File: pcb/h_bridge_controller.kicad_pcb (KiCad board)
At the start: 2 copper layers, 118.1 x 55.1 mm, 58 parts, among them P1 PWR_JACK_2.5x5.5, P10 HEADER_02X08_SMD, P11 HEADER_02X08_SMD, P2 HEADER_01X03_SMD_RA, P3 HEADER_01X03_SMD_RA, P4 HEADER_01X03_SMD_RA, P5 HEADER_01X03_SMD_RA, P6 HEADER_01X02_SMD_RA, P7 BNC_DOUBLE_RA, P8 HEADER_02X08_SMD, P9 HEADER_02X08_SMD, SW1 SPST_SLIDE_AS, U1 TLE7230R, U2 TLE7230R, U3 TLE7230R, U4 TLE7230R

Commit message: Progress towards pcb v1.0.
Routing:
- net GND: track 558.3 -> 0.00 mm, vias 1 -> 0
- net VAA: track 217.8 -> 0.00 mm, vias 1 -> 0
- net +5V: track 216.2 -> 0.00 mm, vias 4 -> 0
- net /LED_PWR: track 207.8 -> 0.00 mm, vias 1 -> 0
- net /SCK: track 112.7 -> 0.00 mm, vias 5 -> 0
- net /RESET: track 97.9 -> 0.00 mm, vias 1 -> 0
- net /CS: track 96.8 -> 0.00 mm, vias 2 -> 0
- net /BNC_A: track 91.3 -> 0.00 mm
- net /TX3: track 85.3 -> 0.00 mm
- net /RX0: track 70.0 -> 0.00 mm
- net /RX3: track 65.1 -> 0.00 mm, vias 1 -> 0
- net /MISO: track 62.2 -> 0.00 mm, vias 1 -> 0
- net /SO2: track 61.2 -> 0.00 mm
- net /TX0: track 58.4 -> 0.00 mm
- net /BNC_B: track 56.7 -> 0.00 mm
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- removed copper zone on B.Cu, net GND
- removed copper zone on F.Cu, net VAA
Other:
- board text added: "Janelia Modular Device h_bridge_controller model_number: 1170 03/2016 ver 1.0"
- board text removed: "Janelia Modular Device h_bridge_controller model_number: 1110 03/2016 ver 1.5"

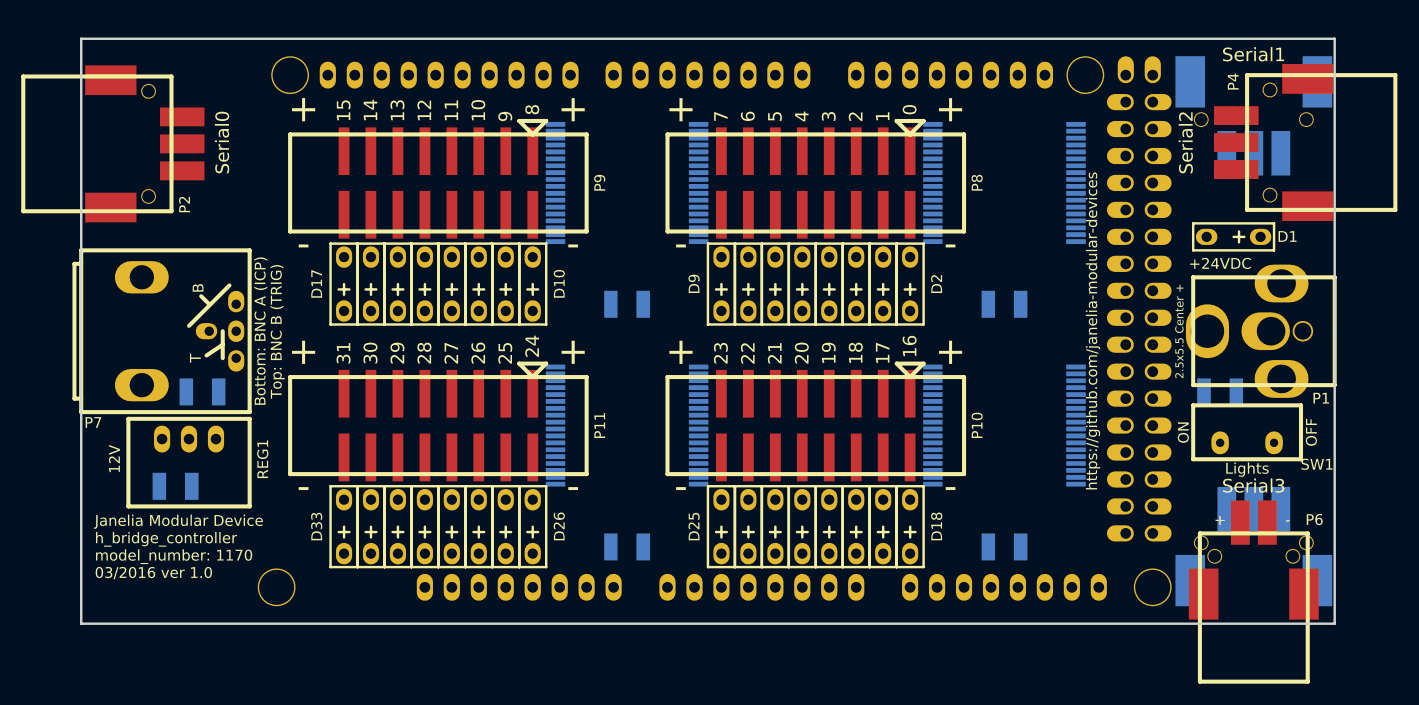
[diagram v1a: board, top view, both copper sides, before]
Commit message: Use relay_controller as pcb base.
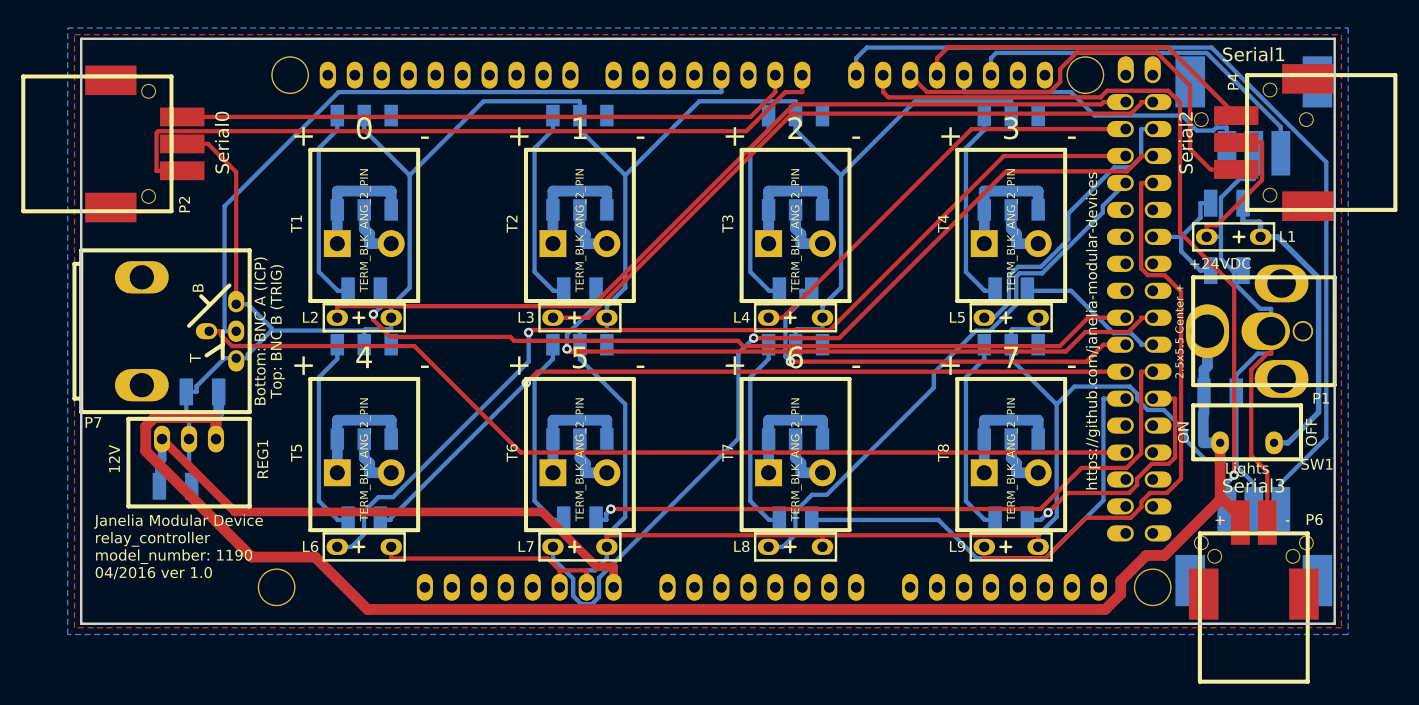
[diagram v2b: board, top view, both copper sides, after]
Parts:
- removed C4, C5, C6, C7: 0.1uF, h_bridge_controller:SM1210
- removed D1, D10, D11, D12, D13, D14, D15, D16, D17, D18, D19, D2, D20, D21, D22, D23, D24, D25, D26, D27, D28, D29, D3, D30, D31, D32, D33, D4, D5, D6, D7, D8, D9: LED_24V, h_bridge_controller:LED_555-3XXX
- removed P10, P11, P8, P9: HEADER_02X08_SMD, h_bridge_controller:HEADER_02x08_SMD
- added L1: LED_24V, relay_controller:LED_555-3XXX, F.Cu at (201.9, 94.0)
- added L2: LED_5V_GRN, relay_controller:LED_555-3XXX, F.Cu at (120.0, 101.6)
- added L3: LED_5V_GRN, relay_controller:LED_555-3XXX, F.Cu at (140.3, 101.6)
- added L4: LED_5V_GRN, relay_controller:LED_555-3XXX, F.Cu at (160.7, 101.6)
- added L5: LED_5V_GRN, relay_controller:LED_555-3XXX, F.Cu at (181.0, 101.6)
- added L6: LED_5V_GRN, relay_controller:LED_555-3XXX, F.Cu at (120.0, 123.2)
- added L7: LED_5V_GRN, relay_controller:LED_555-3XXX, F.Cu at (140.3, 123.2)
- added L8: LED_5V_GRN, relay_controller:LED_555-3XXX, F.Cu at (160.7, 123.2)
- added L9: LED_5V_GRN, relay_controller:LED_555-3XXX, F.Cu at (181.0, 123.2)
- added R1: 5.11k, relay_controller:SM1210, B.Cu at (201.3, 90.8)
- added R10: 150, relay_controller:SM1210, B.Cu at (181.0, 120.7)
- added R2: 1k, relay_controller:SM1210, B.Cu at (201.3, 97.2)
- added R3: 150, relay_controller:SM1210, B.Cu at (120.0, 99.1)
- added R4: 150, relay_controller:SM1210, B.Cu at (140.3, 99.1)
- added R5: 150, relay_controller:SM1210, B.Cu at (160.7, 99.1)
- added R6: 150, relay_controller:SM1210, B.Cu at (181.0, 99.1)
- added R7: 150, relay_controller:SM1210, B.Cu at (120.0, 120.7)
- added R8: 150, relay_controller:SM1210, B.Cu at (140.3, 120.7)
- added R9: 150, relay_controller:SM1210, B.Cu at (160.7, 120.7)
- added T1: TERM_BLK_ANG_2_PIN, relay_controller:TERM_BLK_ANG_2_PIN, F.Cu at (120.0, 94.6)
- added T2: TERM_BLK_ANG_2_PIN, relay_controller:TERM_BLK_ANG_2_PIN, F.Cu at (140.3, 94.6)
- added T3: TERM_BLK_ANG_2_PIN, relay_controller:TERM_BLK_ANG_2_PIN, F.Cu at (160.7, 94.6)
- added T4: TERM_BLK_ANG_2_PIN, relay_controller:TERM_BLK_ANG_2_PIN, F.Cu at (181.0, 94.6)
- added T5: TERM_BLK_ANG_2_PIN, relay_controller:TERM_BLK_ANG_2_PIN, F.Cu at (120.0, 116.2)
- added T6: TERM_BLK_ANG_2_PIN, relay_controller:TERM_BLK_ANG_2_PIN, F.Cu at (140.3, 116.2)
- added T7: TERM_BLK_ANG_2_PIN, relay_controller:TERM_BLK_ANG_2_PIN, F.Cu at (160.7, 116.2)
- added T8: TERM_BLK_ANG_2_PIN, relay_controller:TERM_BLK_ANG_2_PIN, F.Cu at (181.0, 116.2)
- added U5: SSR_DC_6PIN, relay_controller:ASSR-1611, B.Cu at (120.0, 108.6)
- added U6: SSR_DC_6PIN, relay_controller:ASSR-1611, B.Cu at (140.3, 108.6)
- added U7: SSR_DC_6PIN, relay_controller:ASSR-1611, B.Cu at (160.7, 108.6)
- added U8: SSR_DC_6PIN, relay_controller:ASSR-1611, B.Cu at (181.0, 108.6)
- ARDUINO1: footprint h_bridge_controller:ARDUINO_MEGA_SHIELD -> relay_controller:ARDUINO_MEGA_SHIELD
- C1, C2, C3: footprint h_bridge_controller:SM1210 -> relay_controller:SM1210
- P1: footprint h_bridge_controller:DCJACK_2PIN_HIGHCURRENT -> relay_controller:DCJACK_2PIN_HIGHCURRENT
- P2, P3, P4, P5: footprint h_bridge_controller:Header_3_Pin_SMD_RA -> relay_controller:Header_3_Pin_SMD_RA
- P6: footprint h_bridge_controller:Header_2_Pin_SMD_RA -> relay_controller:Header_2_Pin_SMD_RA
- P7: footprint h_bridge_controller:BNC_DOUBLE -> relay_controller:BNC_DOUBLE
- REG1: footprint h_bridge_controller:DC_DC_CONV_R78C -> relay_controller:DC_DC_CONV_R78C
- SW1: footprint h_bridge_controller:SPST_SLIDE_AS -> relay_controller:SPST_SLIDE_AS
- U1, U2, U3, U4: value TLE7230R -> SSR_DC_6PIN; footprint h_bridge_controller:PG-DSO-36 -> relay_controller:ASSR-1611
- moved U1 60.4 mm to (120.0, 87.0)
- moved U4 43.9 mm to (181.0, 87.0)
- moved U3 31.6 mm to (160.7, 87.0)
- moved U2 4.84 mm to (140.3, 87.0)
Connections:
- ARDUINO1 pad 22: (no net) -> /LED_0
- ARDUINO1 pad 23: (no net) -> /LED_1
- ARDUINO1 pad 24: (no net) -> /LED_2
- ARDUINO1 pad 25: (no net) -> /LED_3
- ARDUINO1 pad 26: (no net) -> /LED_4
- ARDUINO1 pad 27: (no net) -> /LED_5
- ARDUINO1 pad 28: (no net) -> /LED_6
- ARDUINO1 pad 29: (no net) -> /LED_7
- ARDUINO1 pad 33: (no net) -> /LED_PWR_IN
- ARDUINO1 pad 38: (no net) -> /RELAY_0
- ARDUINO1 pad 39: (no net) -> /RELAY_1
- ARDUINO1 pad 40: (no net) -> /RELAY_2
- ARDUINO1 pad 41: (no net) -> /RELAY_3
- ARDUINO1 pad 42: (no net) -> /RELAY_4
- ARDUINO1 pad 43: (no net) -> /RELAY_5
- ARDUINO1 pad 44: /RESET -> /RELAY_6
- ARDUINO1 pad 45: (no net) -> /RELAY_7
- ARDUINO1 pad 46: /CS -> (no net)
- ARDUINO1 pad 50: /MISO -> (no net)
- ARDUINO1 pad 51: /MOSI -> (no net)
- ARDUINO1 pad 52: /SCK -> (no net)
- ARDUINO1 pad 5V_1: +5V -> (no net)
- U1 pad 1: GND -> Net-(R3-Pad1)
- U1 pad 2: (no net) -> GND
- U1 pad 4: /OUT0 -> /OUT_0+
- U1 pad 5: /OUT1 -> /OUT_0-
- U1 pad 6: GND -> /OUT_0+
- U2 pad 1: GND -> Net-(R4-Pad1)
- U2 pad 2: (no net) -> GND
- U2 pad 4: /OUT8 -> /OUT_1+
- U2 pad 5: /OUT9 -> /OUT_1-
- U2 pad 6: GND -> /OUT_1+
- U3 pad 1: GND -> Net-(R5-Pad1)
- U3 pad 2: (no net) -> GND
- U3 pad 4: /OUT16 -> /OUT_2+
- U3 pad 5: /OUT17 -> /OUT_2-
- U3 pad 6: GND -> /OUT_2+
- U4 pad 1: GND -> Net-(R6-Pad1)
- U4 pad 2: (no net) -> GND
- U4 pad 4: /OUT24 -> /OUT_3+
- U4 pad 5: /OUT25 -> /OUT_3-
- U4 pad 6: GND -> /OUT_3+
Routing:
- net GND: track 0.00 -> 410.8 mm
- net VAA: track 0.00 -> 149.0 mm
- net /LED_4: track 0.00 -> 92.4 mm, vias 0 -> 1
- net /BNC_A: track 0.00 -> 91.3 mm
- net /TX3: track 0.00 -> 85.2 mm
- net /LED_5: track 0.00 -> 83.6 mm, vias 0 -> 1
- net /LED_0: track 0.00 -> 83.4 mm
- net /RELAY_4: track 0.00 -> 76.1 mm, vias 0 -> 1
- net /RELAY_0: track 0.00 -> 76.1 mm, vias 0 -> 1
- net /RX3: track 0.00 -> 71.2 mm, vias 0 -> 1
- net /RX0: track 0.00 -> 70.0 mm
- net /BNC_B: track 0.00 -> 65.7 mm
- net /LED_1: track 0.00 -> 65.0 mm
- net /RELAY_1: track 0.00 -> 63.4 mm, vias 0 -> 1
- net /RELAY_5: track 0.00 -> 63.1 mm, vias 0 -> 1
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- added copper zone on B.Cu, net GND
- added copper zone on F.Cu, net GND
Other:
- board text added: "Janelia Modular Device relay_controller model_number: 1190 04/2016 ver 1.0"
- board text removed: "10"
- board text removed: "11"
- board text removed: "12"
- board text removed: "13"
- board text removed: "14"
- board text removed: "15"
- board text removed: "16"
- board text removed: "17"
- board text removed: "18"
- board text removed: "19"
- board text removed: "20"
- board text removed: "21"
- board text removed: "22"
- board text removed: "23"
- board text removed: "24"
- board text removed: "25"
- board text removed: "26"
- board text removed: "27"
- board text removed: "28"
- board text removed: "29"
- board text removed: "30"
- board text removed: "31"
- board text removed: "8"
- board text removed: "9"
- board text removed: "Janelia Modular Device h_bridge_controller model_number: 1170 03/2016 ver 1.0"

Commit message: relay_controller -> h_bridge_controller.
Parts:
- ARDUINO1: footprint relay_controller:ARDUINO_MEGA_SHIELD -> h_bridge_controller:ARDUINO_MEGA_SHIELD
- C1, C2, C3, R1, R10, R2, R3, R4, R5, R6, R7, R8, R9: footprint relay_controller:SM1210 -> h_bridge_controller:SM1210
- L1, L2, L3, L4, L5, L6, L7, L8, L9: footprint relay_controller:LED_555-3XXX -> h_bridge_controller:LED_555-3XXX
- P1: footprint relay_controller:DCJACK_2PIN_HIGHCURRENT -> h_bridge_controller:DCJACK_2PIN_HIGHCURRENT
- P2, P3, P4, P5: footprint relay_controller:Header_3_Pin_SMD_RA -> h_bridge_controller:Header_3_Pin_SMD_RA
- P6: footprint relay_controller:Header_2_Pin_SMD_RA -> h_bridge_controller:Header_2_Pin_SMD_RA
- P7: footprint relay_controller:BNC_DOUBLE -> h_bridge_controller:BNC_DOUBLE
- REG1: footprint relay_controller:DC_DC_CONV_R78C -> h_bridge_controller:DC_DC_CONV_R78C
- SW1: footprint relay_controller:SPST_SLIDE_AS -> h_bridge_controller:SPST_SLIDE_AS
- T1, T2, T3, T4, T5, T6, T7, T8: footprint relay_controller:TERM_BLK_ANG_2_PIN -> h_bridge_controller:TERM_BLK_ANG_2_PIN
- U1, U2, U3, U4, U5, U6, U7, U8: footprint relay_controller:ASSR-1611 -> h_bridge_controller:ASSR-1611
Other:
- board text added: "Janelia Modular Device h_bridge_controller model_number: 1190 04/2016 ver 1.0"
- board text removed: "Janelia Modular Device relay_controller model_number: 1190 04/2016 ver 1.0"

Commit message: Progress towards pcb1.0.
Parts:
- removed R10, R5, R6: 150, h_bridge_controller:SM1210
- removed T5, T6, T7, T8: TERM_BLK_ANG_2_PIN, h_bridge_controller:TERM_BLK_ANG_2_PIN
- removed U3, U4, U5, U6, U7, U8: SSR_DC_6PIN, h_bridge_controller:ASSR-1611
- added C4: 0.1uF, h_bridge_controller:SM1210, B.Cu at (121.3, 108.0)
- added C5: 0.1uF, h_bridge_controller:SM1210, B.Cu at (142.9, 108.0)
- added C6: 47uF, h_bridge_controller:SM2917_POL, B.Cu at (114.3, 108.0)
- added C7: 0.1uF, h_bridge_controller:SM1210, B.Cu at (158.8, 108.0)
- added C8: 0.1uF, h_bridge_controller:SM1210, B.Cu at (181.0, 108.0)
- added C9: 47uF, h_bridge_controller:SM2917_POL, B.Cu at (151.8, 108.0)
- added D1: diode_schottky_40V_1A, h_bridge_controller:DO-214AC(SMA), B.Cu at (119.4, 87.6)
- added D10: diode_schottky_40V_1A, h_bridge_controller:DO-214AC(SMA), B.Cu at (157.5, 99.1)
- added D11: diode_schottky_40V_1A, h_bridge_controller:DO-214AC(SMA), B.Cu at (162.6, 87.6)
- added D12: diode_schottky_40V_1A, h_bridge_controller:DO-214AC(SMA), B.Cu at (162.6, 99.1)
- added D13: diode_schottky_40V_1A, h_bridge_controller:DO-214AC(SMA), B.Cu at (176.5, 87.6)
- added D14: diode_schottky_40V_1A, h_bridge_controller:DO-214AC(SMA), B.Cu at (176.5, 99.1)
- added D15: diode_schottky_40V_1A, h_bridge_controller:DO-214AC(SMA), B.Cu at (181.6, 87.6)
- added D16: diode_schottky_40V_1A, h_bridge_controller:DO-214AC(SMA), B.Cu at (181.6, 99.1)
- added D2: diode_schottky_40V_1A, h_bridge_controller:DO-214AC(SMA), B.Cu at (119.4, 99.1)
- added D3: diode_schottky_40V_1A, h_bridge_controller:DO-214AC(SMA), B.Cu at (124.5, 87.6)
- added D4: diode_schottky_40V_1A, h_bridge_controller:DO-214AC(SMA), B.Cu at (124.5, 99.1)
- added D5: diode_schottky_40V_1A, h_bridge_controller:DO-214AC(SMA), B.Cu at (138.4, 87.6)
- added D6: diode_schottky_40V_1A, h_bridge_controller:DO-214AC(SMA), B.Cu at (138.4, 99.1)
- added D7: diode_schottky_40V_1A, h_bridge_controller:DO-214AC(SMA), B.Cu at (143.5, 87.6)
- added D8: diode_schottky_40V_1A, h_bridge_controller:DO-214AC(SMA), B.Cu at (143.5, 99.1)
- added D9: diode_schottky_40V_1A, h_bridge_controller:DO-214AC(SMA), B.Cu at (157.5, 87.6)
- added P10: HEADER_01X05_SMD_SHR, h_bridge_controller:Header_Shrouded_5_Pin_SMD, F.Cu at (175.9, 115.6)
- added P8: HEADER_01X05_SMD_SHR, h_bridge_controller:Header_Shrouded_5_Pin_SMD, F.Cu at (125.1, 115.6)
- added P9: HEADER_01X05_SMD_SHR, h_bridge_controller:Header_Shrouded_5_Pin_SMD, F.Cu at (150.5, 115.6)
- L2, L3, L4, L5, L6, L7, L8, L9: value LED_5V_GRN -> LED_24V
- R1: value 5.11k -> 0.5_2010; footprint h_bridge_controller:SM1210 -> h_bridge_controller:SM2010
- R2: value 1k -> 0.5_2010; footprint h_bridge_controller:SM1210 -> h_bridge_controller:SM2010
- R3, R4: value 150 -> 0.5_2010; footprint h_bridge_controller:SM1210 -> h_bridge_controller:SM2010
- R7, R8, R9: value 150 -> 180
- U1, U2: value SSR_DC_6PIN -> L298; footprint h_bridge_controller:ASSR-1611 -> h_bridge_controller:POWERSO20
- moved R1 84.4 mm to (120.7, 115.6), turned to 270 degrees
- moved R2 61.9 mm to (142.2, 115.6), turned to 270 degrees
- moved L6 46.3 mm to (153.0, 90.8), turned to 0 degrees
- moved R4 43.3 mm to (180.3, 115.6), turned to 270 degrees
- moved R3 42.4 mm to (158.8, 116.2), turned to 270 degrees
- moved L7 42.0 mm to (167.0, 90.8), turned to 0 degrees
- moved U2 37.5 mm to (169.5, 110.5), turned to 90 degrees
- moved L5 34.7 mm to (148.0, 90.8), turned to 0 degrees
- moved L8 34.3 mm to (172.1, 90.8), turned to 0 degrees
- moved L9 32.8 mm to (186.1, 90.8), turned to 0 degrees
- moved L4 28.8 mm to (134.0, 90.8), turned to 0 degrees
- moved U1 26.1 mm to (131.4, 110.5), turned to 90 degrees
- moved R9 17.9 mm to (178.4, 122.6), turned to 180 degrees
- moved L3 15.7 mm to (128.9, 90.8), turned to 0 degrees
- moved R8 12.8 mm to (153.0, 122.6), turned to 180 degrees
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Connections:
- ARDUINO1 pad 10: (no net) -> /PWM_2
- ARDUINO1 pad 11: (no net) -> /PWM_3
- ARDUINO1 pad 2: (no net) -> /SW_2
- ARDUINO1 pad 20: (no net) -> /SW_1
- ARDUINO1 pad 21: (no net) -> /SW_0
- ARDUINO1 pad 22: /LED_0 -> /DIR_0A
- ARDUINO1 pad 23: /LED_1 -> /DIR_0B
- ARDUINO1 pad 24: /LED_2 -> /DIR_1A
- ARDUINO1 pad 25: /LED_3 -> /DIR_1B
- ARDUINO1 pad 26: /LED_4 -> /DIR_2A
- ARDUINO1 pad 27: /LED_5 -> /DIR_2B
- ARDUINO1 pad 28: /LED_6 -> /DIR_3A
- ARDUINO1 pad 29: /LED_7 -> /DIR_3B
- ARDUINO1 pad 33: /LED_PWR_IN -> (no net)
- ARDUINO1 pad 38: /RELAY_0 -> (no net)
- ARDUINO1 pad 39: /RELAY_1 -> (no net)
- ARDUINO1 pad 40: /RELAY_2 -> (no net)
- ARDUINO1 pad 41: /RELAY_3 -> (no net)
- ARDUINO1 pad 42: /RELAY_4 -> (no net)
- ARDUINO1 pad 43: /RELAY_5 -> (no net)
- ARDUINO1 pad 44: /RELAY_6 -> (no net)
- ARDUINO1 pad 45: /RELAY_7 -> (no net)
- ARDUINO1 pad 5V_1: (no net) -> +5V
- ARDUINO1 pad 8: (no net) -> /PWM_0
- ARDUINO1 pad 9: (no net) -> /PWM_1
- ARDUINO1 pad A0: (no net) -> /SENSE_0
- ARDUINO1 pad A1: (no net) -> /SENSE_1
- ARDUINO1 pad A2: (no net) -> /SENSE_2
- ARDUINO1 pad A3: (no net) -> /SENSE_3
- L2 pad 1: /LED_0 -> /LED_PWR
- L2 pad 2: GND -> /OUT_0+
- L3 pad 1: /LED_1 -> /LED_PWR
- L3 pad 2: GND -> /OUT_0-
- L4 pad 1: /LED_2 -> /LED_PWR
- L4 pad 2: GND -> /OUT_1+
- L5 pad 1: /LED_3 -> /LED_PWR
- L5 pad 2: GND -> /OUT_1-
- L6 pad 1: /LED_4 -> /LED_PWR
- L6 pad 2: GND -> /OUT_2+
- L7 pad 1: /LED_5 -> /LED_PWR
- L7 pad 2: GND -> /OUT_2-
- L8 pad 1: /LED_6 -> /LED_PWR
- L8 pad 2: GND -> /OUT_3+
- L9 pad 1: /LED_7 -> /LED_PWR
- L9 pad 2: GND -> /OUT_3-
- R1 pad 1: /LED_PWR -> /SENSE_0
- R1 pad 2: /LED_PWR_IN -> GND
- R2 pad 1: /LED_PWR_IN -> /SENSE_1
- R3 pad 1: Net-(R3-Pad1) -> /SENSE_2
- R3 pad 2: /RELAY_0 -> GND
- R4 pad 1: Net-(R4-Pad1) -> /SENSE_3
- R4 pad 2: /RELAY_1 -> GND
- R7 pad 2: /RELAY_4 -> +5V
- R8 pad 2: /RELAY_5 -> +5V
- R9 pad 2: /RELAY_6 -> +5V
- U1 pad 1: Net-(R3-Pad1) -> GND
- U1 pad 2: GND -> /SENSE_0
- U1 pad 6: /OUT_0+ -> VAA
- U2 pad 1: Net-(R4-Pad1) -> GND
- U2 pad 2: GND -> /SENSE_2
- U2 pad 4: /OUT_1+ -> /OUT_2+
- U2 pad 5: /OUT_1- -> /OUT_2-
- U2 pad 6: /OUT_1+ -> VAA
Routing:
- net GND: track 410.8 -> 0.00 mm
- net VAA: track 149.0 -> 0.00 mm
- net /LED_4: track 92.4 -> 0.00 mm, vias 1 -> 0
- net /BNC_A: track 91.3 -> 0.00 mm
- net /TX3: track 85.2 -> 0.00 mm
- net /LED_5: track 83.6 -> 0.00 mm, vias 1 -> 0
- net /LED_0: track 83.4 -> 0.00 mm
- net /RELAY_4: track 76.1 -> 0.00 mm, vias 1 -> 0
- net /RELAY_0: track 76.1 -> 0.00 mm, vias 1 -> 0
- net /RX3: track 71.2 -> 0.00 mm, vias 1 -> 0
- net /RX0: track 70.0 -> 0.00 mm
- net /BNC_B: track 65.7 -> 0.00 mm
- net /LED_1: track 65.0 -> 0.00 mm
- net /RELAY_1: track 63.4 -> 0.00 mm, vias 1 -> 0
- net /RELAY_5: track 63.1 -> 0.00 mm, vias 1 -> 0
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- removed copper zone on B.Cu, net GND
- removed copper zone on F.Cu, net GND
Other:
- board text added: "Janelia Modular Device h_bridge_controller model_number: 1170 04/2016 ver 1.0"
- board text removed: "2"
- board text removed: "3"
- board text removed: "4"
- board text removed: "5"
- board text removed: "6"
- board text removed: "7"
- board text removed: "Janelia Modular Device h_bridge_controller model_number: 1190 04/2016 ver 1.0"

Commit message: More progress towards pcb1.0.
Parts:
- R1, R2, R3, R4: value 0.5_2010 -> 0.5
- moved L2 5.08 mm to (114.9, 95.9)
- moved L3 5.08 mm to (128.9, 95.9)
- moved L4 5.08 mm to (134.0, 95.9)
- moved L5 5.08 mm to (148.0, 95.9)
- moved L6 5.08 mm to (153.0, 95.9)
- moved L7 5.08 mm to (167.0, 95.9)
- moved L8 5.08 mm to (172.1, 95.9)
- moved L9 5.08 mm to (186.1, 95.9)
- moved C8 2.62 mm to (181.6, 105.4)
- moved C5 2.62 mm to (143.5, 105.4)
- moved C4 2.01 mm to (119.4, 107.3), turned to 90 degrees
- moved C6 2.01 mm to (112.4, 107.3)
- moved R3 1.80 mm to (157.5, 114.9), turned to 180 degrees
- moved R1 1.42 mm to (119.4, 114.9), turned to 180 degrees
- moved R4 1.42 mm to (181.6, 114.9), turned to 0 degrees
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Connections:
- net /PWM_0 renamed /ENABLE_0
- net /PWM_1 renamed /ENABLE_1
- net /PWM_2 renamed /ENABLE_2
- net /PWM_3 renamed /ENABLE_3
- L1 pad 1: /LED_PWR -> VAA
- L1 pad 2: GND -> /LED_GND
- L2 pad 1: /LED_PWR -> /OUT_0+
- L2 pad 2: /OUT_0+ -> /LED_GND
- L3 pad 1: /LED_PWR -> /OUT_0-
- L3 pad 2: /OUT_0- -> /LED_GND
- L4 pad 1: /LED_PWR -> /OUT_1+
- L4 pad 2: /OUT_1+ -> /LED_GND
- L5 pad 1: /LED_PWR -> /OUT_1-
- L5 pad 2: /OUT_1- -> /LED_GND
- L6 pad 1: /LED_PWR -> /OUT_2+
- L6 pad 2: /OUT_2+ -> /LED_GND
- L7 pad 1: /LED_PWR -> /OUT_2-
- L7 pad 2: /OUT_2- -> /LED_GND
- L8 pad 1: /LED_PWR -> /OUT_3+
- L8 pad 2: /OUT_3+ -> /LED_GND
- L9 pad 1: /LED_PWR -> /OUT_3-
- L9 pad 2: /OUT_3- -> /LED_GND
- SW1 pad 1: VAA -> GND
- SW1 pad 3: /LED_PWR -> /LED_GND

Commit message: Finished pcb1.0.
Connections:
- ARDUINO1 pad 22: /DIR_0A -> (no net)
- ARDUINO1 pad 23: /DIR_0B -> (no net)
- ARDUINO1 pad 24: /DIR_1A -> (no net)
- ARDUINO1 pad 25: /DIR_1B -> (no net)
- ARDUINO1 pad 26: /DIR_2A -> (no net)
- ARDUINO1 pad 27: /DIR_2B -> (no net)
- ARDUINO1 pad 28: /DIR_3A -> (no net)
- ARDUINO1 pad 29: /DIR_3B -> (no net)
- ARDUINO1 pad 30: (no net) -> /DIR_0A
- ARDUINO1 pad 31: (no net) -> /DIR_0B
- ARDUINO1 pad 32: (no net) -> /DIR_1A
- ARDUINO1 pad 33: (no net) -> /DIR_1B
- ARDUINO1 pad 34: (no net) -> /DIR_2A
- ARDUINO1 pad 35: (no net) -> /DIR_2B
- ARDUINO1 pad 36: (no net) -> /DIR_3A
- ARDUINO1 pad 37: (no net) -> /DIR_3B
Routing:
- net GND: track 0.00 -> 495.5 mm, vias 0 -> 5
- net VAA: track 0.00 -> 248.3 mm, vias 0 -> 2
- net /LED_GND: track 0.00 -> 158.2 mm, vias 0 -> 1
- net +5V: track 0.00 -> 130.1 mm, vias 0 -> 3
- net /SW_0: track 0.00 -> 123.0 mm
- net /SW_1: track 0.00 -> 99.7 mm, vias 0 -> 1
- net /BNC_A: track 0.00 -> 93.2 mm
- net /ENABLE_3: track 0.00 -> 91.1 mm
- net /TX3: track 0.00 -> 86.4 mm
- net /DIR_0A: track 0.00 -> 79.8 mm, vias 0 -> 1
- net /DIR_0B: track 0.00 -> 79.2 mm, vias 0 -> 1
- net /ENABLE_2: track 0.00 -> 78.4 mm, vias 0 -> 1
- net /SW_2: track 0.00 -> 75.9 mm, vias 0 -> 1
- net /RX0: track 0.00 -> 70.0 mm
- net /RX3: track 0.00 -> 65.0 mm
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- added copper zone on F.Cu, net GND
- added copper zone on B.Cu, net VAA
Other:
- board text added: "2"
- board text added: "3"
